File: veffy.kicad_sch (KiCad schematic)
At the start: 149 parts, among them CN1 XH-2AW_C2908611, J1 SWD, J2 Conn_Coaxial, J3 USB_C_Receptacle_USB2.0_14P, Q1 2N7002, Q2 BFR93A, Q3 2N7002, Q4 BFR93AE6327HTSA1, SW1 SW_Push, SW2 SW_Push, U1 ATSAMD21G18A-A, U10 MC34063AD, U11 AP2112K-3.3, U2 ADF4112BCPZ, U3 SA612AN/01_112, U4 MC3361, U5 LM386, U6 LM358_DFN, U7 AD9834, U8 QPA9510, U9 MCP73831-2-OT, Y2 C7527392

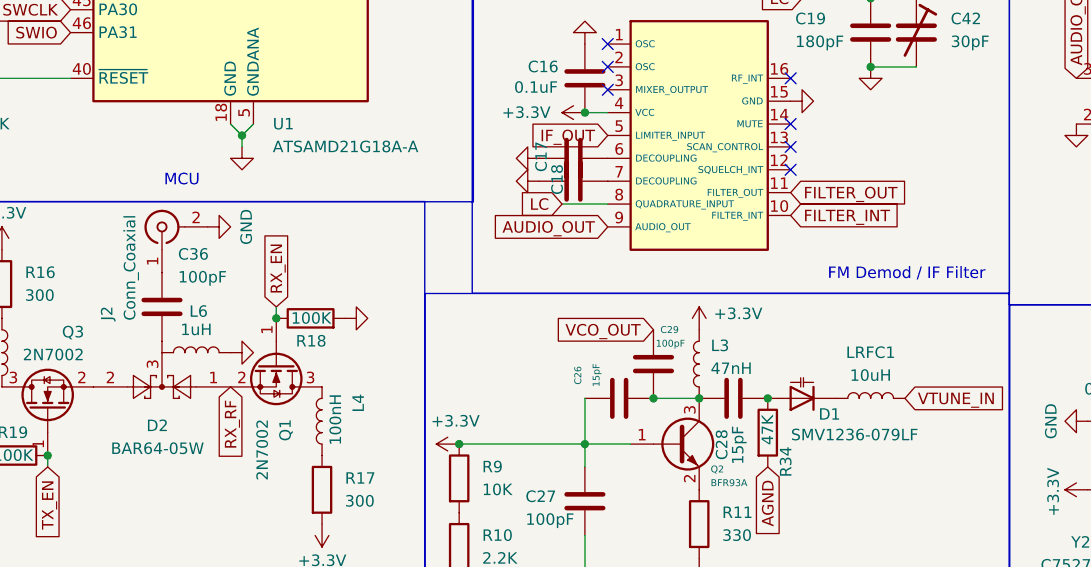
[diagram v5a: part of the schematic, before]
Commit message: fixed footprints and some schematic errors
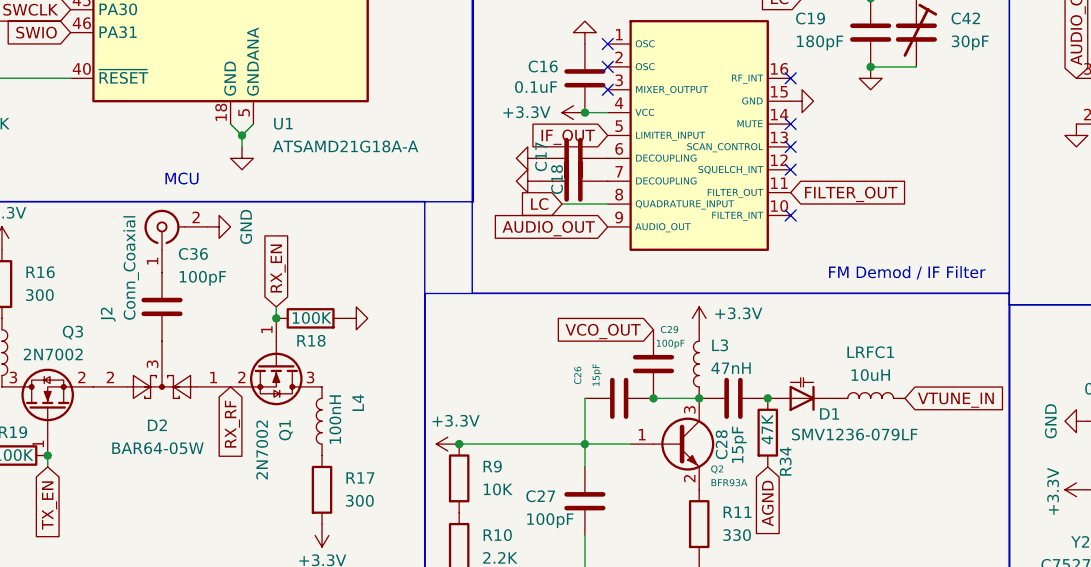
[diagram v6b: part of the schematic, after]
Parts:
- removed L6: 1uH, Inductor_SMD:L_0603_1608Metric, symbol Device:L
- C42, C51, C52, C53, C54, C55, C56, C57, C58, C59, C60, C61, C62, C63, FB1: footprint (none) -> Capacitor_SMD:C_0603_1608Metric_Pad1.08x0.95mm_HandSolder
- J2: footprint (none) -> Connector_Coaxial:SMA_Amphenol_901-144_Vertical
- L15, L17, L18, L19: footprint (none) -> Inductor_SMD:L_0603_1608Metric_Pad1.05x0.95mm_HandSolder
- L16: footprint Inductor_SMD:L_0603_1608Metric -> Inductor_SMD:L_0603_1608Metric_Pad1.05x0.95mm_HandSolder
- R29, R30, R31, R32, R33, R34, R35: footprint (none) -> Resistor_SMD:R_0603_1608Metric_Pad0.98x0.95mm_HandSolder
- SW1, SW2: footprint (none) -> Button_Switch_SMD:SW_MEC_5GSH9
- U6: footprint Package_CSP:LFCSP-8_2x2mm_P0.5mm -> Package_DFN_QFN:DFN-8-1EP_2x2mm_P0.5mm_EP1.05x1.75mm
- Y2: footprint OSC-SMD_4P-L2.0-W1.6-BL_EPSON_TG-5006CJ-19H -> LCSC:OSC-SMD_4P-L2.0-W1.6-BL_EPSON_TG-5006CJ-19H
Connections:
- net FILTER_INT: no longer names the net of U4.10 (FILTER_INT)
- no-connect marks 17 -> 18

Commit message: worked on the PCB and fixed some schematic issues
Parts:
- added C64: 1nF, symbol Device:C
- added R36: 680, Resistor_SMD:R_0603_1608Metric_Pad0.98x0.95mm_HandSolder, symbol Device:R
- C7: value 100pF -> 10pF
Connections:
- net INPUTB: now reaches C7.2, U3.2 (INPUTB)
- net INPUTB: now also C64.2, R36.1
- net at R14.1: now also R36.2; no longer U7.19 (IOUT)
- new net: C64.1, U7.19 (IOUT)
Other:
- moved on the sheet: R14

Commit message: mic amp fixes
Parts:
- added C68: 1uF, symbol Device:C
- added C69: 10nF, symbol Device:C
- added R37: 1K, symbol Device:R
- C21: value 10uF -> 4.7uF; footprint Capacitor_SMD:C_0603_1608Metric_Pad1.08x0.95mm_HandSolder -> (none)
- C25: value 1uF -> 1nF; footprint Capacitor_SMD:C_0603_1608Metric_Pad1.08x0.95mm_HandSolder -> (none)
- C64: footprint (none) -> Capacitor_SMD:C_0603_1608Metric
- C65, C66, C67: footprint (none) -> Capacitor_SMD:C_Trimmer_Murata_TZB4-A
- D1: footprint (none) -> LCSC:SC-79_L1.2-W0.8-LS1.6-RD
- R6: value 15K -> 47K
- U6: value LM358_DFN -> TLV9062IDSGR
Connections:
- net GND: now also C21.2, C69.2; no longer R7.2
- net MIC_PREAMP: now also U6.5 (+), C68.2; no longer C25.1
- net PRE_AMP: now also C25.2, R37.1; no longer C21.2
- net at R6.1, R7.1, U6.6 (-): now also C25.1
- net at MK1.2 (+), R3.1: now also C68.1; no longer C21.1
- net at U1.9 (PA04): now also C69.1, R37.2
- new net: C21.1, R7.2
